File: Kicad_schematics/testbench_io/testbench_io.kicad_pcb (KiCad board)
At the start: 2 copper layers, 183 x 130 mm, 75 parts, among them J101 Conn_01x02, J102 Conn_01x02, J103 Conn_01x02, J104 DB37_Female_MountingHoles, J301 Conn_01x04, J302 Conn_01x04, J303 Conn_01x04, Q201 2N3904, Q301 IPD50R380CE, Q302 IPD50R380CE, Q303 IPD50R380CE, Q304 IPD50R380CE, Q305 IPD50R380CE, Q306 IPD50R380CE, SW101 SW_SPST, SW102 SW_Push, SW103 SW_Push, SW104 SW_Push, SW105 SW_Push, SW106 SW_SPST, SW107 SW_SPST, SW108 SW_DIP_x08, SW109 SW_SPST, SW110 SW_Push, SW111 SW_SPST, SW112 SW_SPST, SW113 SW_SPST, SW114 SW_DPDT_x2, SW201 SW_DIP_x01, U101 NUCLEO64-F476RG, U102 CJMCU_MCP2551, U201 PCF8574AN

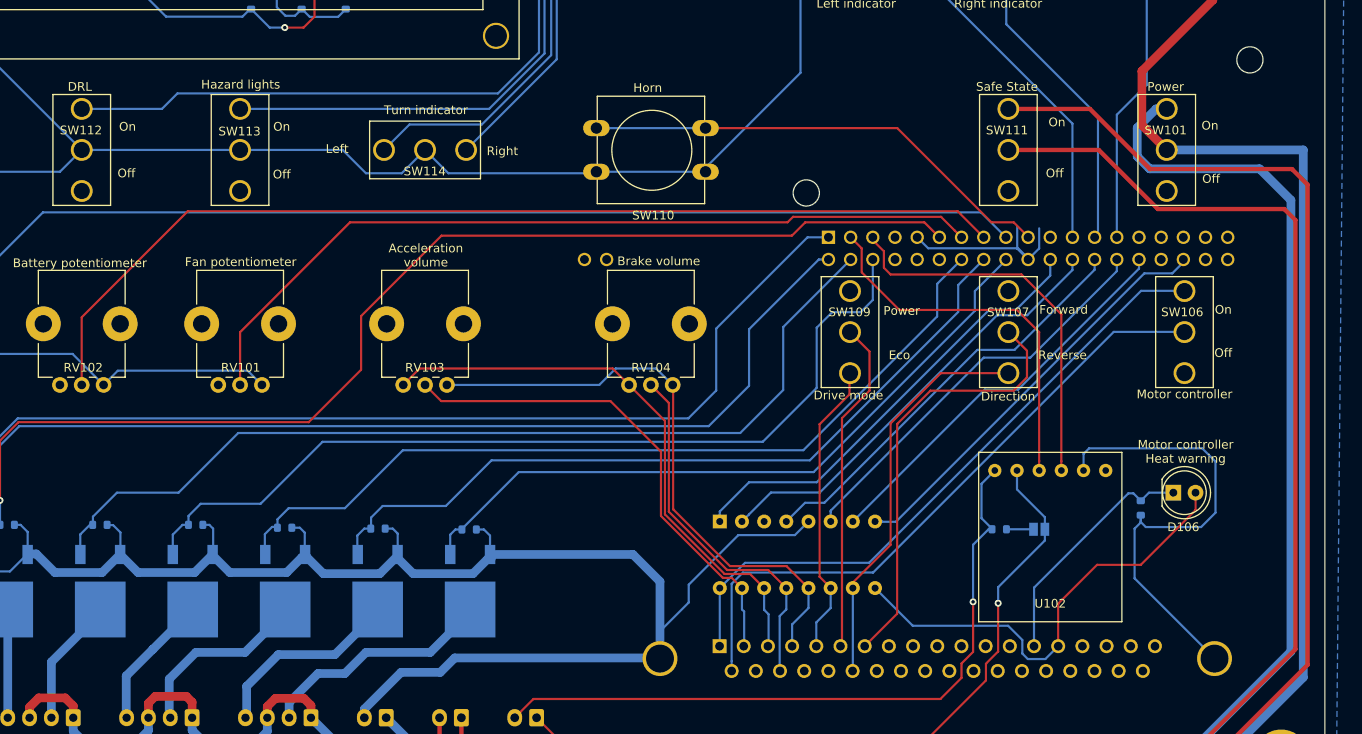
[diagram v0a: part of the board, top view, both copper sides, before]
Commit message: Edited some footprints to cheaper ones.
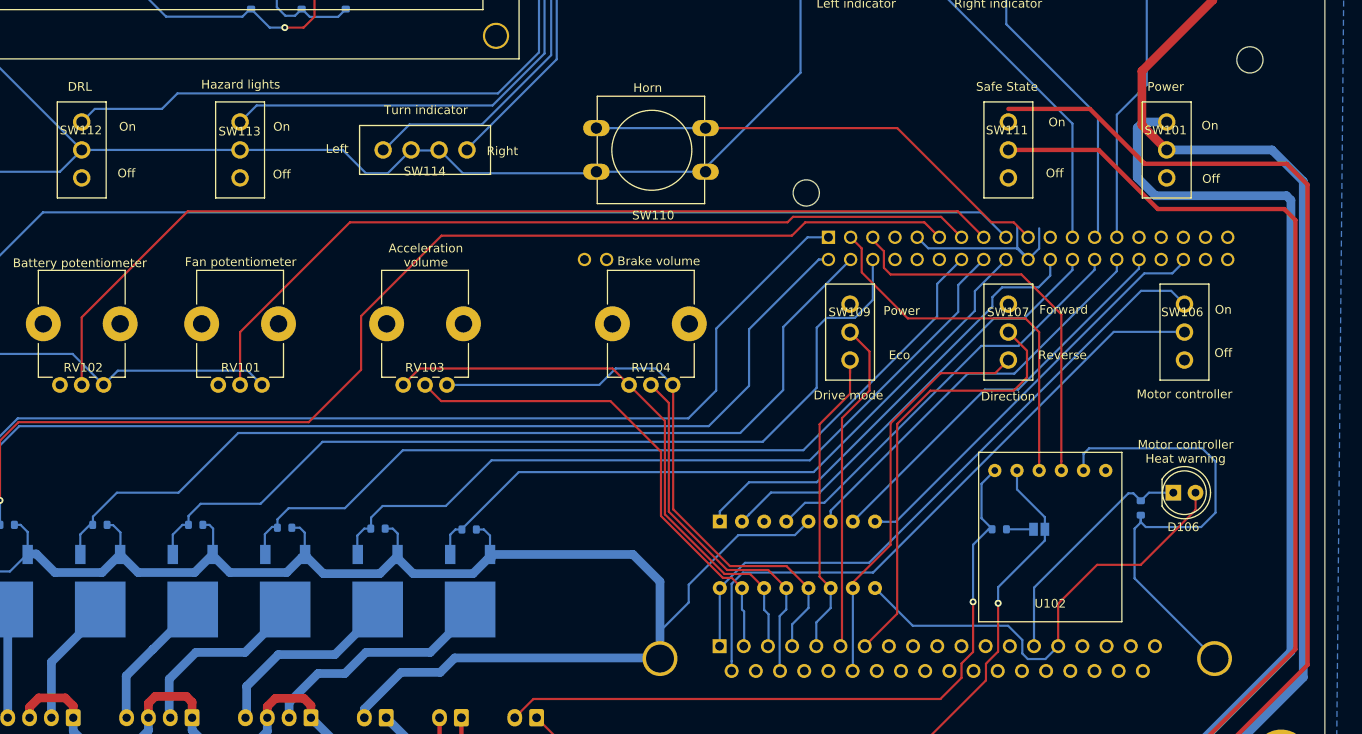
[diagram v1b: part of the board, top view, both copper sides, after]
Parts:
- SW101, SW106, SW107, SW109, SW111, SW112, SW113: footprint Solar_team:RND-Slide-Switch -> Solar_team:MFP120
- SW114: footprint Solar_team:RND-Slide-Switch -> Solar_team:MFP130
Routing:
- net /TRM_05: track 33.9 -> 36.9 mm
- net VDD_MCU: track 313.7 -> 311.6 mm
- net V_external: track 190.1 -> 190.9 mm
- net /MC_sw: track 52.0 -> 52.7 mm
- net /TRM_01: track 74.0 -> 74.6 mm
- net /TRM_25: track 46.0 -> 46.7 mm
- net /HL_sw: track 129.7 -> 130.4 mm
- net /DRL_sw: track 151.2 -> 151.8 mm

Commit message: Fixed gerbers
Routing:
- net GND: track 797.0 -> 792.1 mm
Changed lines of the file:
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@@
     (thickness 1.6)
     (drawings 51)
-    (tracks 832)
+    (tracks 830)
     (zones 0)
     (modules 75)
@@
   (segment (start 68.834 39.593) (end 70.739 37.688) (width 0.25) (layer B.Cu) (net 2))
   (segment (start 67.564 39.593) (end 68.834 39.593) (width 0.25) (layer B.Cu) (net 2) (status 10))
-  (segment (start 127.2666 125.2036) (end 127.2666 134.0278) (width 1) (layer B.Cu) (net 2) (status 20))
-  (segment (start 124.1716 122.1086) (end 127.2666 125.2036) (width 1) (layer B.Cu) (net 2))
-  (segment (start 107.8058 122.1086) (end 124.1716 122.1086) (width 1) (layer B.Cu) (net 2) (status 10))
   (segment (start 45.266 140.859) (end 48.641 137.484) (width 0.25) (layer B.Cu) (net 2) (status 10))
   (segment (start 48.641 137.484) (end 48.641 124.937) (width 0.25) (layer B.Cu) (net 2))
@@
   (segment (start 182.3212 118.3894) (end 182.3212 117.6086) (width 0.25) (layer B.Cu) (net 2))
   (segment (start 175.768 112.491) (end 175.768 110.586) (width 0.25) (layer B.Cu) (net 2))
-  (segment (start 130.556 127.6096) (end 127.2666 130.899) (width 0.25) (layer B.Cu) (net 2))
-  (segment (start 127.2666 130.899) (end 127.2666 134.0278) (width 0.25) (layer B.Cu) (net 2))
-  (segment (start 130.556 125.572) (end 130.556 127.6096) (width 0.25) (layer B.Cu) (net 2))
-  (segment (start 136.24 119.888) (end 130.556 125.572) (width 0.25) (layer B.Cu) (net 2))
-  (segment (start 142.717 119.888) (end 136.24 119.888) (width 0.25) (layer B.Cu) (net 2))
-  (segment (start 144.272 118.333) (end 142.717 119.888) (width 0.25) (layer B.Cu) (net 2))
   (segment (start 49.467 52.9458) (end 49.467 51.658) (width 0.25) (layer B.Cu) (net 2))
   (segment (start 48.705 53.7078) (end 49.467 52.9458) (width 0.25) (layer B.Cu) (net 2))
@@
   (segment (start 90.9278 75.7838) (end 93.599 78.455) (width 0.25) (layer B.Cu) (net 2))
   (segment (start 79.183 75.7838) (end 90.9278 75.7838) (width 0.25) (layer B.Cu) (net 2))
+  (segment (start 127.2666 133.4642) (end 127.2666 134.0278) (width 1) (layer B.Cu) (net 2))
+  (segment (start 115.911 122.1086) (end 127.2666 133.4642) (width 1) (layer B.Cu) (net 2))
+  (segment (start 107.8058 122.1086) (end 115.911 122.1086) (width 1) (layer B.Cu) (net 2))
+  (segment (start 127.2666 128.8614) (end 127.2666 134.0278) (width 0.25) (layer B.Cu) (net 2))
+  (segment (start 136.24 119.888) (end 127.2666 128.8614) (width 0.25) (layer B.Cu) (net 2))
+  (segment (start 142.717 119.888) (end 136.24 119.888) (width 0.25) (layer B.Cu) (net 2))
+  (segment (start 144.272 118.333) (end 142.717 119.888) (width 0.25) (layer B.Cu) (net 2))
   (segment (start 145.415 54.007) (end 145.415 54.8076) (width 0.25) (layer B.Cu) (net 3) (status 10))
   (segment (start 145.5674 54.96) (end 148.293666 54.96) (width 0.25) (layer B.Cu) (net 3) (status 20))
